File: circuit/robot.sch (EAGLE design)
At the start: 15 parts, among them M1 SERVO-FLIPPED, M2 SERVO-1, M3 SERVO-1, U1 ESP01

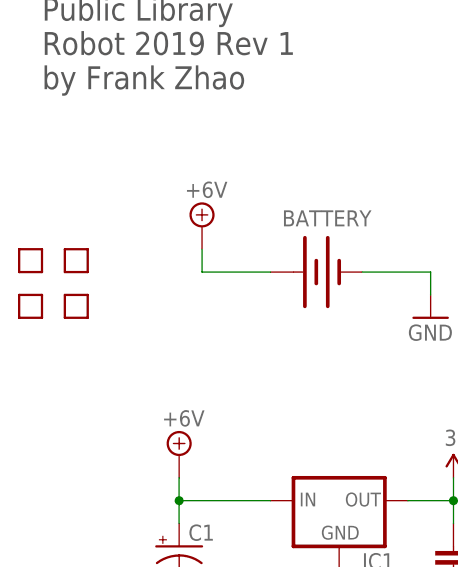
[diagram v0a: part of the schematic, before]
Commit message: smaller pcb
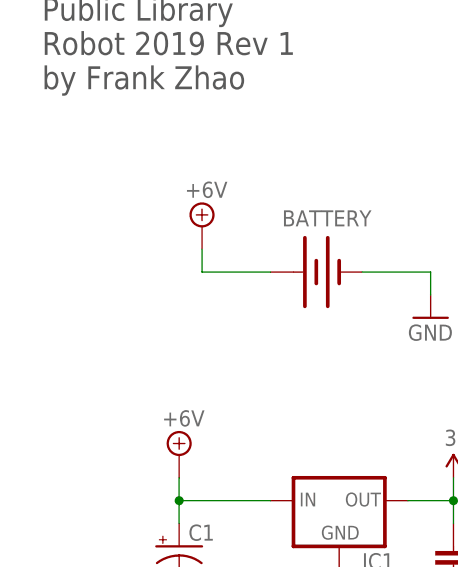
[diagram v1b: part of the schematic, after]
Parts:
- removed U$10, U$11, U$12, U$13: HOLE, robot:HOLE
- R1: device robot:RESISTORAXIAL-0.3 -> robot:RESISTORAXIAL-0.3-NOVAL
- U$9: value TEXT-INFO -> TEXT-INFO-INVISIBLE; device robot:TEXT-INFO -> robot:TEXT-INFO-INVISIBLE
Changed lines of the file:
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@@
 <grid distance="0.1" unitdist="inch" unit="inch" style="lines" multiple="1" display="no" altdistance="0.01" altunitdist="inch" altunit="inch"/>
 <layers>
-<layer number="1" name="Top" color="4" fill="1" visible="no" active="no"/>
-<layer number="2" name="Route2" color="1" fill="3" visible="no" active="no"/>
-<layer number="3" name="Route3" color="4" fill="3" visible="no" active="no"/>
-<layer number="4" name="Route4" color="1" fill="4" visible="no" active="no"/>
-<layer number="5" name="Route5" color="4" fill="4" visible="no" active="no"/>
-<layer number="6" name="Route6" color="1" fill="8" visible="no" active="no"/>
-<layer number="7" name="Route7" color="4" fill="8" visible="no" active="no"/>
-<layer number="8" name="Route8" color="1" fill="2" visible="no" active="no"/>
-<layer number="9" name="Route9" color="4" fill="2" visible="no" active="no"/>
-<layer number="10" name="Route10" color="1" fill="7" visible="no" active="no"/>
-<layer number="11" name="Route11" color="4" fill="7" visible="no" active="no"/>
-<layer number="12" name="Route12" color="1" fill="5" visible="no" active="no"/>
-<layer number="13" name="Route13" color="4" fill="5" visible="no" active="no"/>
-<layer number="14" name="Route14" color="1" fill="6" visible="no" active="no"/>
-<layer number="15" name="Route15" color="4" fill="6" visible="no" active="no"/>
-<layer number="16" name="Bottom" color="1" fill="1" visible="no" active="no"/>
-<layer number="17" name="Pads" color="2" fill="1" visible="no" active="no"/>
-<layer number="18" name="Vias" color="2" fill="1" visible="no" active="no"/>
-<layer number="19" name="Unrouted" color="6" fill="1" visible="no" active="no"/>
-<layer number="20" name="Dimension" color="15" fill="1" visible="no" active="no"/>
-<layer number="21" name="tPlace" color="7" fill="1" visible="no" active="no"/>
-<layer number="22" name="bPlace" color="7" fill="1" visible="no" active="no"/>
-<layer number="23" name="tOrigins" color="15" fill="1" visible="no" active="no"/>
-<layer number="24" name="bOrigins" color="15" fill="1" visible="no" active="no"/>
-<layer number="25" name="tNames" color="7" fill="1" visible="no" active="no"/>
-<layer number="26" name="bNames" color="7" fill="1" visible="no" active="no"/>
-<layer number="27" name="tValues" color="7" fill="1" visible="no" active="no"/>
-<layer number="28" name="bValues" color="7" fill="1" visible="no" active="no"/>
+<layer number="1" name="Top" color="4" fill="1" visible="yes" active="no"/>
+<layer number="2" name="Route2" color="1" fill="3" visible="yes" active="no"/>
+<layer number="3" name="Route3" color="4" fill="3" visible="yes" active="no"/>
+<layer number="4" name="Route4" color="1" fill="4" visible="yes" active="no"/>
+<layer number="5" name="Route5" color="4" fill="4" visible="yes" active="no"/>
+<layer number="6" name="Route6" color="1" fill="8" visible="yes" active="no"/>
+<layer number="7" name="Route7" color="4" fill="8" visible="yes" active="no"/>
+<layer number="8" name="Route8" color="1" fill="2" visible="yes" active="no"/>
+<layer number="9" name="Route9" color="4" fill="2" visible="yes" active="no"/>
+<layer number="10" name="Route10" color="1" fill="7" visible="yes" active="no"/>
+<layer number="11" name="Route11" color="4" fill="7" visible="yes" active="no"/>
+<layer number="12" name="Route12" color="1" fill="5" visible="yes" active="no"/>
+<layer number="13" name="Route13" color="4" fill="5" visible="yes" active="no"/>
+<layer number="14" name="Route14" color="1" fill="6" visible="yes" active="no"/>
+<layer number="15" name="Route15" color="4" fill="6" visible="yes" active="no"/>
+<layer number="16" name="Bottom" color="1" fill="1" visible="yes" active="no"/>
+<layer number="17" name="Pads" color="2" fill="1" visible="yes" active="no"/>
+<layer number="18" name="Vias" color="2" fill="1" visible="yes" active="no"/>
+<layer number="19" name="Unrouted" color="6" fill="1" visible="yes" active="no"/>
+<layer number="20" name="Dimension" color="15" fill="1" visible="yes" active="no"/>
+<layer number="21" name="tPlace" color="7" fill="1" visible="yes" active="no"/>
+<layer number="22" name="bPlace" color="7" fill="1" visible="yes" active="no"/>
+<layer number="23" name="tOrigins" color="15" fill="1" visible="yes" active="no"/>
+<layer number="24" name="bOrigins" color="15" fill="1" visible="yes" active="no"/>
+<layer number="25" name="tNames" color="7" fill="1" visible="yes" active="no"/>
+<layer number="26" name="bNames" color="7" fill="1" visible="yes" active="no"/>
+<layer number="27" name="tValues" color="7" fill="1" visible="yes" active="no"/>
+<layer number="28" name="bValues" color="7" fill="1" visible="yes" active="no"/>
 <layer number="29" name="tStop" color="7" fill="3" visible="no" active="no"/>
 <layer number="30" name="bStop" color="7" fill="6" visible="no" active="no"/>
@@
 <layer number="35" name="tGlue" color="7" fill="4" visible="no" active="no"/>
 <layer number="36" name="bGlue" color="7" fill="5" visible="no" active="no"/>
-<layer number="37" name="tTest" color="7" fill="1" visible="no" active="no"/>
-<layer number="38" name="bTest" color="7" fill="1" visible="no" active="no"/>
+<layer number="37" name="tTest" color="7" fill="1" visible="yes" active="no"/>
+<layer number="38" name="bTest" color="7" fill="1" visible="yes" active="no"/>
 <layer number="39" name="tKeepout" color="4" fill="11" visible="no" active="no"/>
 <layer number="40" name="bKeepout" color="1" fill="11" visible="no" active="no"/>
@@
 <layer number="44" name="Drills" color="7" fill="1" visible="no" active="no"/>
 <layer number="45" name="Holes" color="7" fill="1" visible="no" active="no"/>
-<layer number="46" name="Milling" color="3" fill="1" visible="no" active="no"/>
-<layer number="47" name="Measures" color="7" fill="1" visible="no" active="no"/>
-<layer number="48" name="Document" color="7" fill="1" visible="no" active="no"/>
-<layer number="49" name="Reference" color="7" fill="1" visible="no" active="no"/>
-<layer number="50" name="dxf" color="7" fill="1" visible="no" active="no"/>
-<layer number="51" name="tDocu" color="7" fill="1" visible="no" active="no"/>
-<layer number="52" name="bDocu" color="7" fill="1" visible="no" active="no"/>
-<layer number="53" name="tGND_GNDA" color="7" fill="9" visible="no" active="no"/>
-<layer number="54" name="bGND_GNDA" color="1" fill="9" visible="no" active="no"/>
-<layer number="56" name="wert" color="7" fill="1" visible="no" active="no"/>
+<layer number="46" name="Milling" color="3" fill="1" visible="yes" active="no"/>
+<layer number="47" name="Measures" color="7" fill="1" visible="yes" active="no"/>
+<layer number="48" name="Document" color="7" fill="1" visible="yes" active="no"/>
+<layer number="49" name="Reference" color="7" fill="1" visible="yes" active="no"/>
+<layer number="50" name="dxf" color="7" fill="1" visible="yes" active="no"/>
+<layer number="51" name="tDocu" color="7" fill="1" visible="yes" active="no"/>
+<layer number="52" name="bDocu" color="7" fill="1" visible="yes" active="no"/>
+<layer number="53" name="tGND_GNDA" color="7" fill="9" visible="yes" active="no"/>
+<layer number="54" name="bGND_GNDA" color="1" fill="9" visible="yes" active="no"/>
+<layer number="56" name="wert" color="7" fill="1" visible="yes" active="no"/>
 <layer number="88" name="SimResults" color="9" fill="1" visible="yes" active="yes"/>
 <layer number="89" name="SimProbes" color="9" fill="1" visible="yes" active="yes"/>
@@
 <parts>
 <part name="LED1" library="robot" deviceset="LED" device="5MM"/>
-<part name="R1" library="robot" deviceset="RESISTOR" device="AXIAL-0.3" value="220Ω"/>
+<part name="R1" library="robot" deviceset="RESISTOR" device="AXIAL-0.3-NOVAL" value="220Ω"/>
 <part name="BATTERY" library="robot" deviceset="BATTERY" device="-WIRE-CONN"/>
 <part name="M1" library="robot" deviceset="SERVO" device="-FLIPPED" value="SERVO-FLIPPED"/>
@@
 <part name="GND9" library="robot" deviceset="GND" device=""/>
 <part name="SUPPLY4" library="robot" deviceset="+6V" device=""/>
-<part name="U$9" library="robot" deviceset="TEXT-INFO" device=""/>
-<part name="U$10" library="robot" deviceset="HOLE" device=""/>
-<part name="U$11" library="robot" deviceset="HOLE" device=""/>
-<part name="U$12" library="robot" deviceset="HOLE" device=""/>
-<part name="U$13" library="robot" deviceset="HOLE" device=""/>
+<part name="U$9" library="robot" deviceset="TEXT-INFO" device="-INVISIBLE" value="TEXT-INFO-INVISIBLE"/>
 <part name="U1" library="robot" deviceset="ESP01" device=""/>
 <part name="IC1" library="robot" deviceset="V_REG_78XX" device="TO-92"/>
@@
 <instance part="SUPPLY4" gate="G$1" x="-30.48" y="20.32"/>
 <instance part="U$9" gate="G$1" x="-45.72" y="60.96"/>
-<instance part="U$10" gate="G$1" x="-48.26" y="40.64"/>
-<instance part="U$11" gate="G$1" x="-43.18" y="40.64"/>
-<instance part="U$12" gate="G$1" x="-48.26" y="35.56"/>
-<instance part="U$13" gate="G$1" x="-43.18" y="35.56"/>
 <instance part="U1" gate="G$1" x="38.1" y="-2.54" rot="R180"/>
 <instance part="IC1" gate="G$1" x="-12.7" y="15.24"/>
